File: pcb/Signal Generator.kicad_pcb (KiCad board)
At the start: 2 copper layers, 72 parts, among them J1 AudioJack3, J2 Conn_02x02_Odd_Even, J3 Screw_Terminal_01x04, J4 MEM2080-00-128-00-A, J5 USB_C_Receptacle_USB2.0, J6 Conn_01x04, SW1 SW_Push, SW2 SW_SPDT, U1 FT230XQ, U2 Opamp_Dual, U3 STM32F071RBTx, U4 LD39050PU33R, U5 TLV61048, U6 LDK320AM120R, Y1 TG2520SMN_16.0000M-MCGNNM0

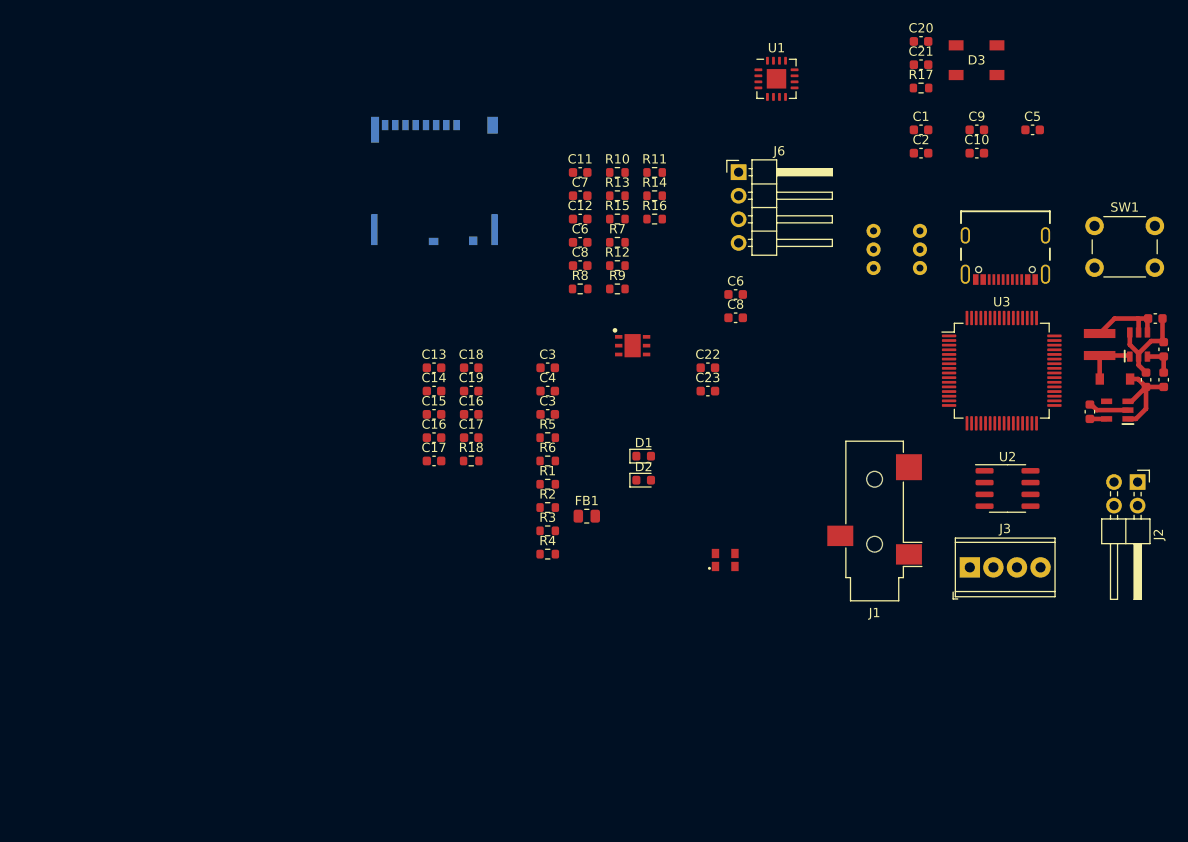
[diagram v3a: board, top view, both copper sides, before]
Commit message: Updated some footprints
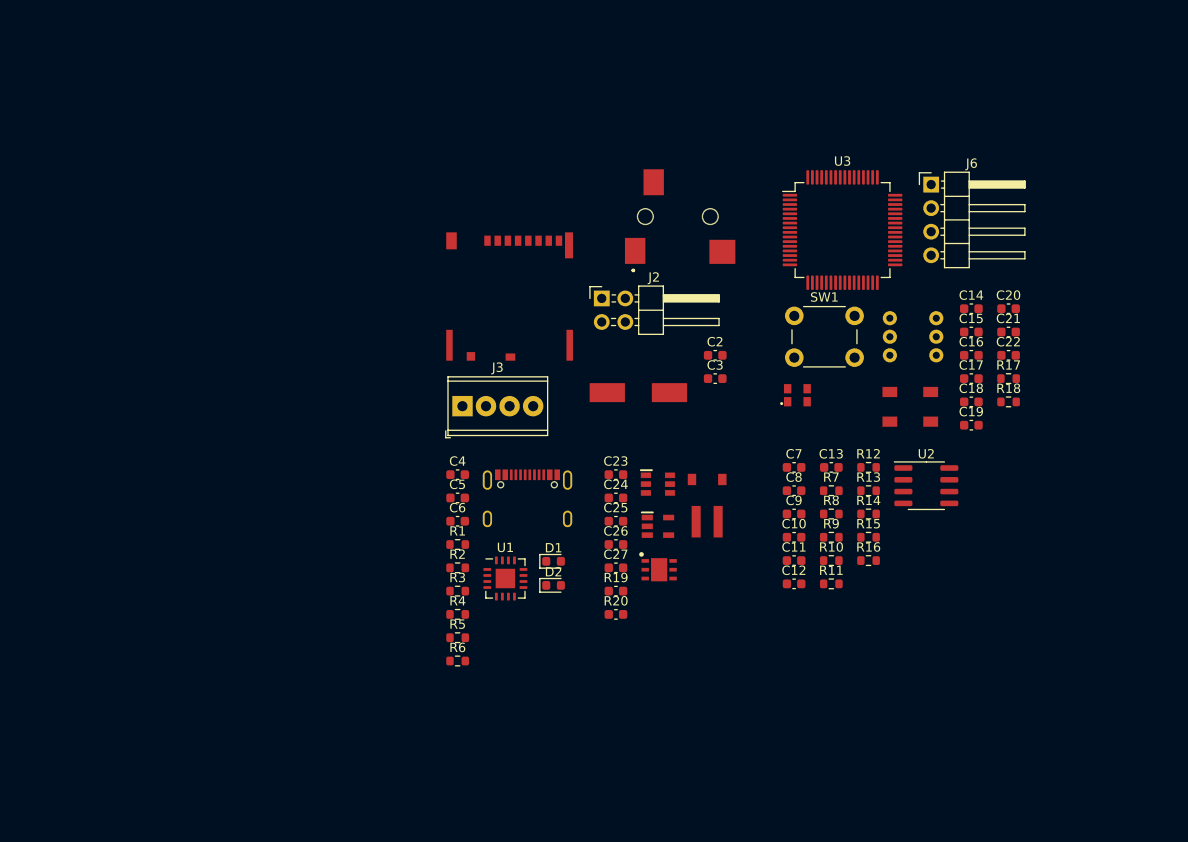
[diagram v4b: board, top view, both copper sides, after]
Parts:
- removed the C16 at (138.7, 113.9)
- removed the C16 at (134.7, 116.4)
- removed the C17 at (138.7, 116.4)
- removed the C17 at (134.7, 118.9)
- removed the C3 at (147.0, 108.9)
- removed the C3 at (147.0, 113.9)
- removed the C6 at (150.5, 95.4)
- removed the C6 at (167.2, 101.0)
- removed the C8 at (167.2, 103.5)
- removed the C8 at (150.5, 97.9)
- removed FB1: FerriteBead, Resistor_SMD:R_0805_2012Metric
- added C16: 100n, Capacitor_SMD:C_0603_1608Metric, F.Cu at (192.6, 107.5)
- added C17: 100n, Capacitor_SMD:C_0603_1608Metric, F.Cu at (192.6, 110.1)
- added C27: 1u, Capacitor_SMD:C_0603_1608Metric, F.Cu at (154.3, 130.4)
- added C3: 100n, Capacitor_SMD:C_0603_1608Metric, F.Cu at (165.0, 110.1)
- added C6: 100n, Capacitor_SMD:C_0603_1608Metric, F.Cu at (137.3, 125.4)
- added C8: 100n, Capacitor_SMD:C_0603_1608Metric, F.Cu at (173.5, 122.1)
- C1: value 10u -> 330u; footprint Capacitor_SMD:C_0603_1608Metric -> Signal Generator Components:WCAP-PSHP
- C10: value 100n -> 100p
- C11: value 6.8u -> 100n
- C12: value 100n -> 6.8u
- C13: value 10n -> 100n
- C14: value 100n -> 10n
- C18, C22: value 1u -> 100n
- C19: value 4.7u -> 1u
- C2: value 100n -> 10u
- C21: value 100n -> 4.7u
- C25: value 10u -> 1u
- C26: value 1u -> 10u
- C5: value 100n -> 47p
- C7: value 100n -> 0.5p
- C9: value 100p -> 0.5p
- J1: footprint Connector_Audio:Jack_3.5mm_CUI_SJ-3523-SMT_Horizontal -> Signal Generator Components:SJ-3523-SMT-TR-1
- J4: moved to F.Cu
- moved C5 73.6 mm to (137.3, 122.9)
- moved R20 65.6 mm to (154.3, 135.5), turned to 0 degrees
- moved R19 63.3 mm to (154.3, 133.0), turned to 0 degrees
- moved U1 61.3 mm to (142.4, 131.6)
- moved C24 61.3 mm to (154.3, 122.9)
- moved J2 61.0 mm to (152.8, 101.4), turned to 0 degrees
- moved J5 59.9 mm to (144.8, 125.2), turned to 0 degrees
- moved C25 59.1 mm to (154.3, 125.4), turned to 0 degrees
- moved C14 58.6 mm to (192.6, 102.5)
- moved C15 58.6 mm to (192.6, 105.0)
- moved R18 58.3 mm to (196.6, 112.6)
- moved J3 57.4 mm to (137.8, 113.0)
- moved C18 54.0 mm to (192.6, 112.6)
- moved C19 54.0 mm to (192.6, 115.1)
- moved U5 53.9 mm to (158.9, 121.4), turned to 0 degrees
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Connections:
- C1 pad 1: +3.3V -> Net-(C1-Pad1)
- C12 pad 1: Net-(U2B-+) -> +12VA
- C13 pad 1: +3.3V -> Net-(U2B-+)
- C21 pad 1: /MCU/NRST -> +3.3V
- C22 pad 1: +5V -> /MCU/NRST
- C23 pad 1: +3.3V -> +5V
- C24 pad 1: +5V -> +3.3V
- C25 pad 1: /Power/13.12V -> +5V
- C26 pad 1: +12VA -> /Power/13.12V
- C4 pad 1: /USB Connector/USB_D- -> /USB Connector/USB_D+
- C5 pad 1: /USB Connector/FT_3V3 -> /USB Connector/USB_D-
- C7 pad 1: Net-(U2A-+) -> /DAC2
- C7 pad 2: GND -> /Output Stage/CH1_OUT
- C9 pad 1: +12VA -> /DAC1
- C9 pad 2: GND -> /Output Stage/CH2_OUT
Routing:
- net GND: track 15.0 -> 0.00 mm
- net /Power/13.12V: track 11.3 -> 0.00 mm
- net +5V: track 8.97 -> 0.00 mm
- net Net-(D4-A): track 5.84 -> 0.00 mm
- net Net-(U5-FB): track 3.34 -> 0.00 mm
- net +12VA: track 1.80 -> 0.00 mm

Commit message: Updated PCB
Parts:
- removed C21: 4.7u, Capacitor_SMD:C_0603_1608Metric
- added C28: 1u, Capacitor_SMD:C_0603_1608Metric, F.Cu at (93.0, 115.5)
- J1: footprint Signal Generator Components:SJ-3523-SMT-TR-1 -> Signal Generator Components:SJ-3523-SMT-TR
- J4, J6: moved to B.Cu
- U3: value STM32F071RBTx -> STM32F103RBTx
- moved R18 95.4 mm to (101.2, 113.2), turned to 90 degrees
- moved C14 95.3 mm to (99.2, 121.5), turned to 90 degrees
- moved C15 94.7 mm to (101.0, 129.0), turned to 135 degrees
- moved C20 94.0 mm to (103.2, 113.2), turned to 90 degrees
- moved C19 93.9 mm to (99.2, 124.8), turned to -90 degrees
- moved C16 92.1 mm to (101.0, 117.0), turned to -135 degrees
- moved SW2 91.9 mm to (91.0, 98.8)
- moved R13 87.5 mm to (94.8, 133.0), turned to 180 degrees
- moved R16 87.0 mm to (94.8, 135.5), turned to -90 degrees
- moved R14 85.5 mm to (96.8, 135.5), turned to 90 degrees
- moved U2 83.2 mm to (105.5, 134.2), turned to 180 degrees
- moved R12 82.3 mm to (100.8, 135.5), turned to -90 degrees
- moved C18 81.3 mm to (113.0, 129.0), turned to 45 degrees
- moved R15 81.0 mm to (100.8, 132.2), turned to 90 degrees
- moved C17 79.9 mm to (113.0, 117.0), turned to 135 degrees
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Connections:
- J2 pad 1: GND -> /Output Stage/CH1_OUT
- J2 pad 2: /Output Stage/CH1_OUT -> GND
- J2 pad 3: GND -> /Output Stage/CH2_OUT
- J2 pad 4: /Output Stage/CH2_OUT -> GND
- U3 pad 24: /MCU/OSC -> unconnected-(U3-PC4-Pad24)
- U3 pad 25: unconnected-(U3-PC5-Pad25) -> /MCU/OSC
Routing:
- net +12VA: track 0.00 -> 51.6 mm, vias 0 -> 2
- net /Output Stage/CH1_OUT: track 0.00 -> 45.2 mm, vias 0 -> 1
- net /Output Stage/CH2_OUT: track 0.00 -> 44.8 mm, vias 0 -> 1
- net /MCU/NRST: track 0.00 -> 37.4 mm, vias 0 -> 1
- net +3.3V: track 0.00 -> 33.7 mm, vias 0 -> 10
- net Net-(C1-Pad1): track 0.00 -> 31.4 mm
- net +5V: track 0.00 -> 29.1 mm, vias 0 -> 9
- net /SD_MISO: track 0.00 -> 26.7 mm, vias 0 -> 1
- net /SD_SCK: track 0.00 -> 25.1 mm, vias 0 -> 1
- net /SD_MOSI: track 0.00 -> 24.1 mm, vias 0 -> 1
- net /MCU/SWDIO: track 0.00 -> 23.6 mm, vias 0 -> 1
- net /SD_CS: track 0.00 -> 22.9 mm, vias 0 -> 2
- net /MCU/SWCLK: track 0.00 -> 22.6 mm, vias 0 -> 1
- net /ADC1: track 0.00 -> 19.4 mm, vias 0 -> 2
- net Net-(SW2-B): track 0.00 -> 18.1 mm, vias 0 -> 1
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- added copper zone on In2.Cu, net +3.3V
- added copper zone on B.Cu, net +5V
- added copper zone on F.Cu, net +5V
- added copper zone on F.Cu, net /Power/13.12V
- added copper zone on F.Cu, net GND
- added copper zone on In1.Cu, net GND
- added copper zone on F.Cu, net Net-(D4-A)
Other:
- board outline added: 36 x 58.5 mm
- copper layers 2 -> 4

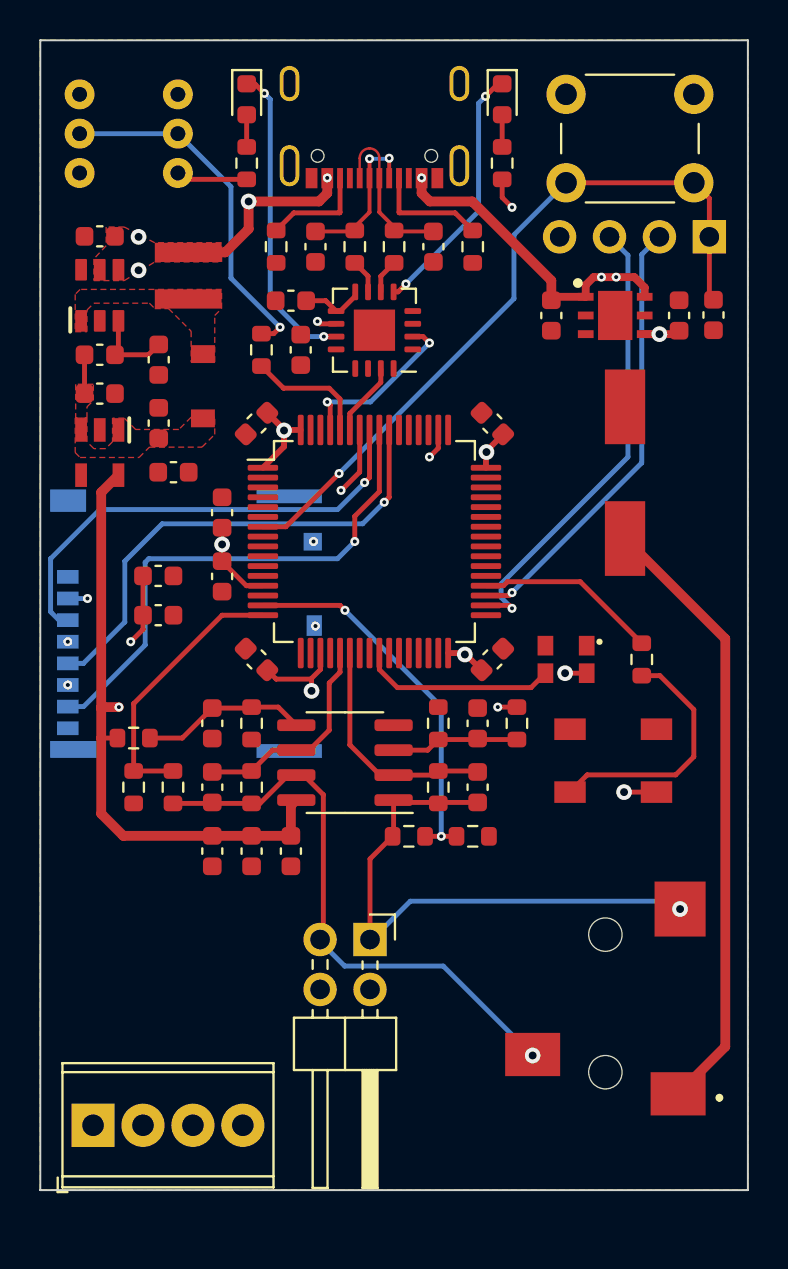
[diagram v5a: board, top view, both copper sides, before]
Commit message: Completed PCB and prepared production files
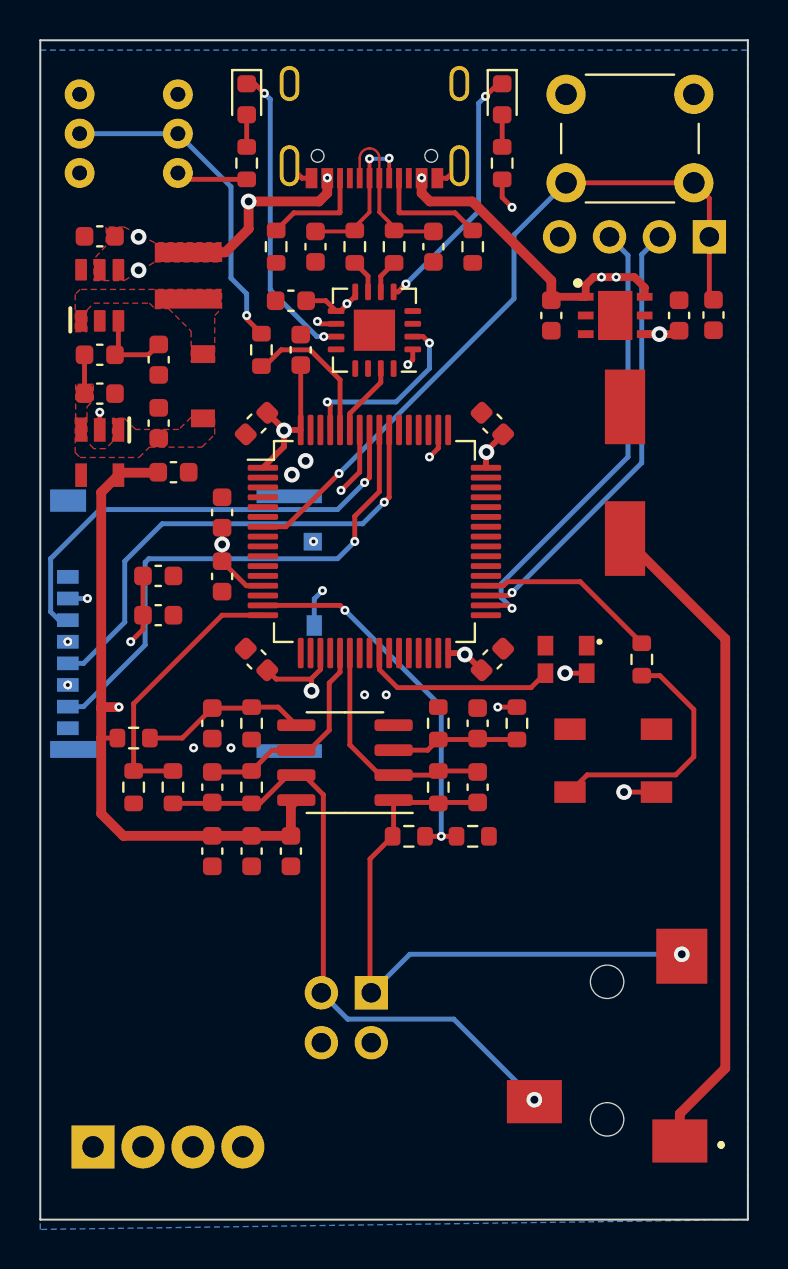
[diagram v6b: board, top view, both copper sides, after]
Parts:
- moved J2 2.71 mm to (106.8, 146.0)
- moved J1 2.40 mm to (118.8, 155.9)
- moved J3 1.10 mm to (92.7, 153.8)
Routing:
- net /USB Connector/FT_3V3: track 3.25 -> 8.53 mm, vias 0 -> 2
- net GND: track 0.00 -> 3.67 mm, vias 2 -> 9
- net +3.3V: track 33.7 -> 37.0 mm
- net Net-(C1-Pad1): track 31.4 -> 33.7 mm
- net +12VA: track 51.6 -> 53.7 mm
- net /Output Stage/CH2_OUT: track 44.8 -> 46.8 mm
- net /Output Stage/CH1_OUT: track 45.2 -> 43.9 mm
- net /MCU/BOOT0: track 6.27 -> 7.53 mm
- net Net-(SW2-B): track 18.1 -> 16.9 mm
- net /MCU/UART1_RX: track 8.91 -> 9.68 mm
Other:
- board size 36 x 58.5 mm -> 36 x 60 mm

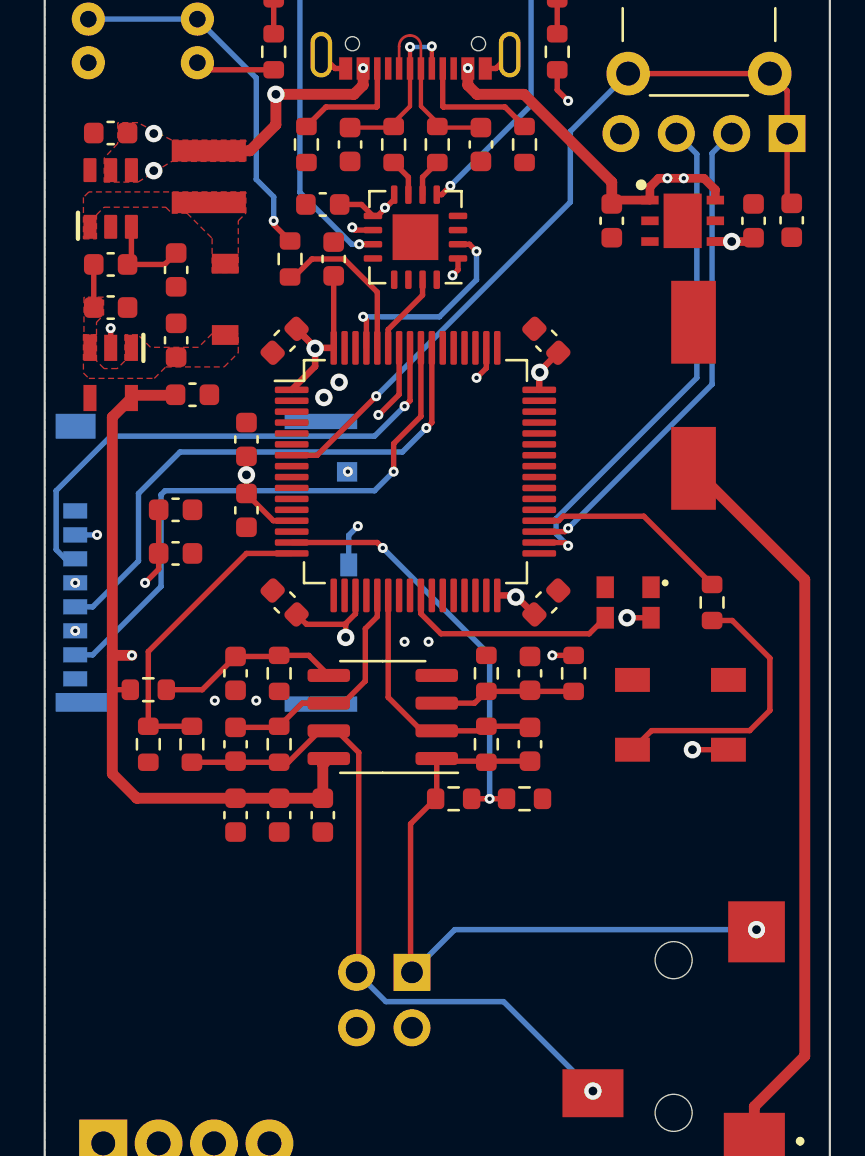
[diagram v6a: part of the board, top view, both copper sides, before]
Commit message: Updated PCB to correct some connection errors
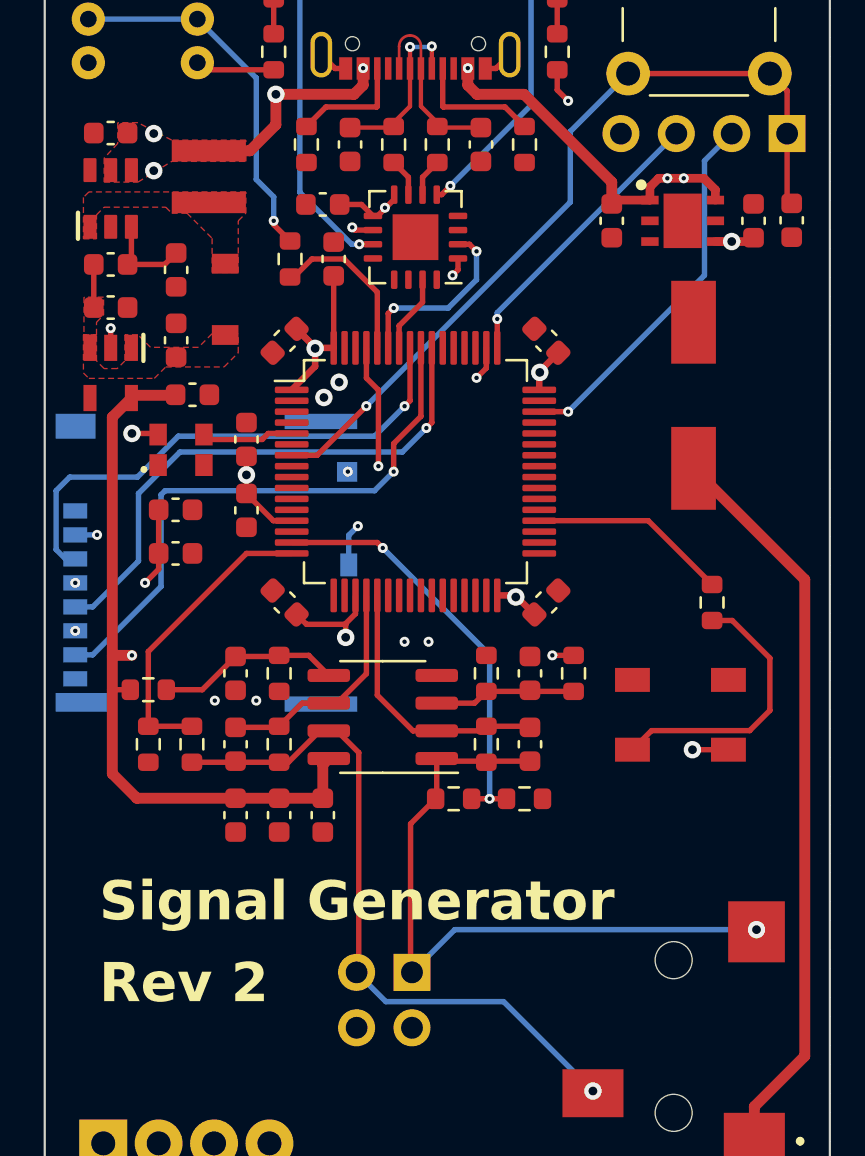
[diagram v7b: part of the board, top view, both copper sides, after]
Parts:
- moved Y1 21.7 mm to (96.2, 122.0), turned to 0 degrees
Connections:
- J6 pad 2: /MCU/SWCLK -> /MCU/SWDIO
- J6 pad 3: /MCU/SWDIO -> /MCU/SWCLK
- U3 pad 20: unconnected-(U3-PA4-Pad20) -> /DAC1
- U3 pad 21: /DAC1 -> /DAC2
- U3 pad 22: /DAC2 -> unconnected-(U3-PA6-Pad22)
- U3 pad 25: /MCU/OSC -> unconnected-(U3-PC5-Pad25)
- U3 pad 34: /MCU/SWDIO -> unconnected-(U3-PB13-Pad34)
- U3 pad 35: /MCU/SWCLK -> unconnected-(U3-PB14-Pad35)
- U3 pad 46: unconnected-(U3-PA13-Pad46) -> /MCU/SWDIO
- U3 pad 49: unconnected-(U3-PA14-Pad49) -> /MCU/SWCLK
- U3 pad 5: unconnected-(U3-PD0-Pad5) -> /MCU/OSC
- U3 pad 58: /SD_Detect -> /MCU/UART1_TX
- U3 pad 59: /MCU/UART1_TX -> /MCU/UART1_RX
- U3 pad 61: /MCU/UART1_RX -> /SD_Detect
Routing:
- net /MCU/SWCLK: track 22.6 -> 13.2 mm
- net /MCU/SWDIO: track 23.6 -> 17.2 mm
- net /MCU/OSC: track 9.98 -> 4.23 mm
- net /MCU/UART1_RX: track 9.68 -> 8.55 mm
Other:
- board text added: "GND SWCLK SWDIO NRST"
- board text added: "Rev 2"
- board text added: "Signal Generator"
